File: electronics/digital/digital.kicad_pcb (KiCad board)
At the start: 2 copper layers, 75 parts, among them J1 USB_A, J2 USB_A, J3 RJ45, P1 POWER_IN, P10 AMP_POWER_OUT, P11 CONTROL, P12 ADC, P2 3V3_IN, P3 USB_CABLE, P4 USB_CABLE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

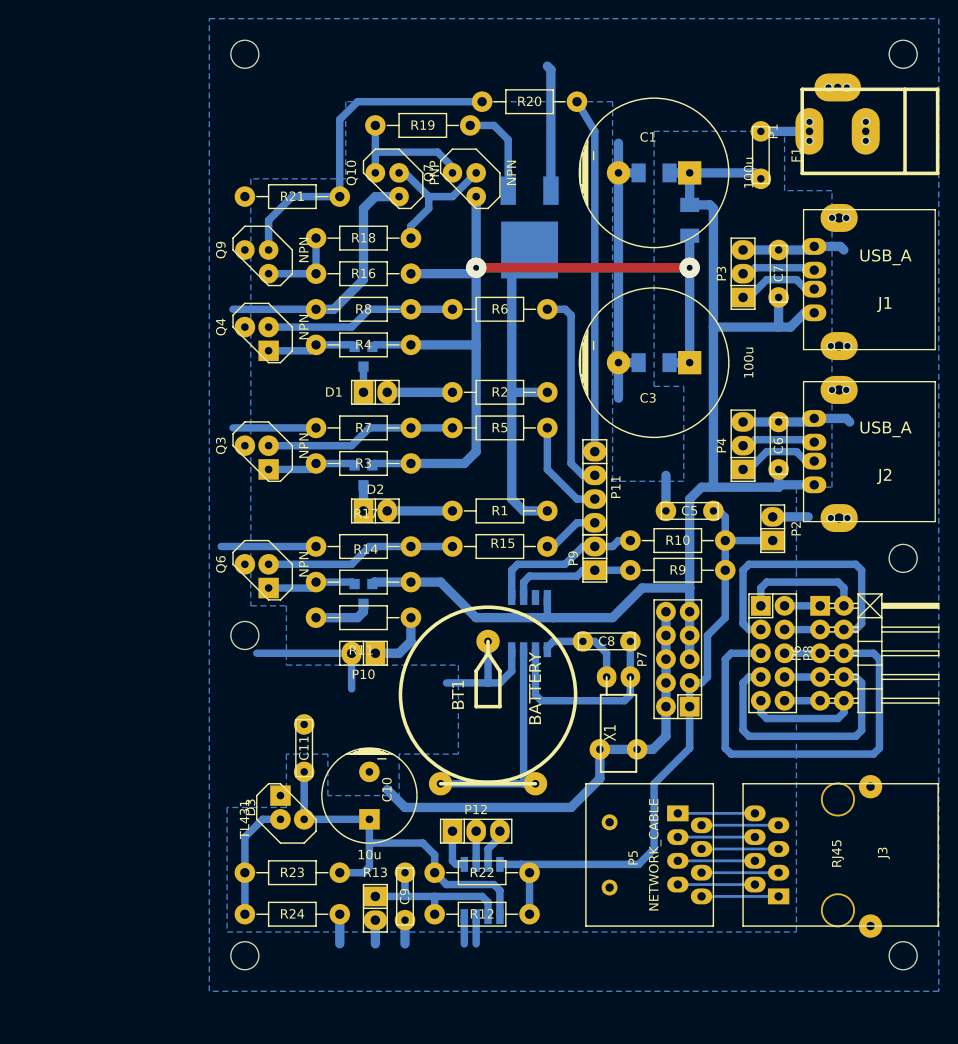
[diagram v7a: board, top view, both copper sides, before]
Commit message: make holes connected to gnd
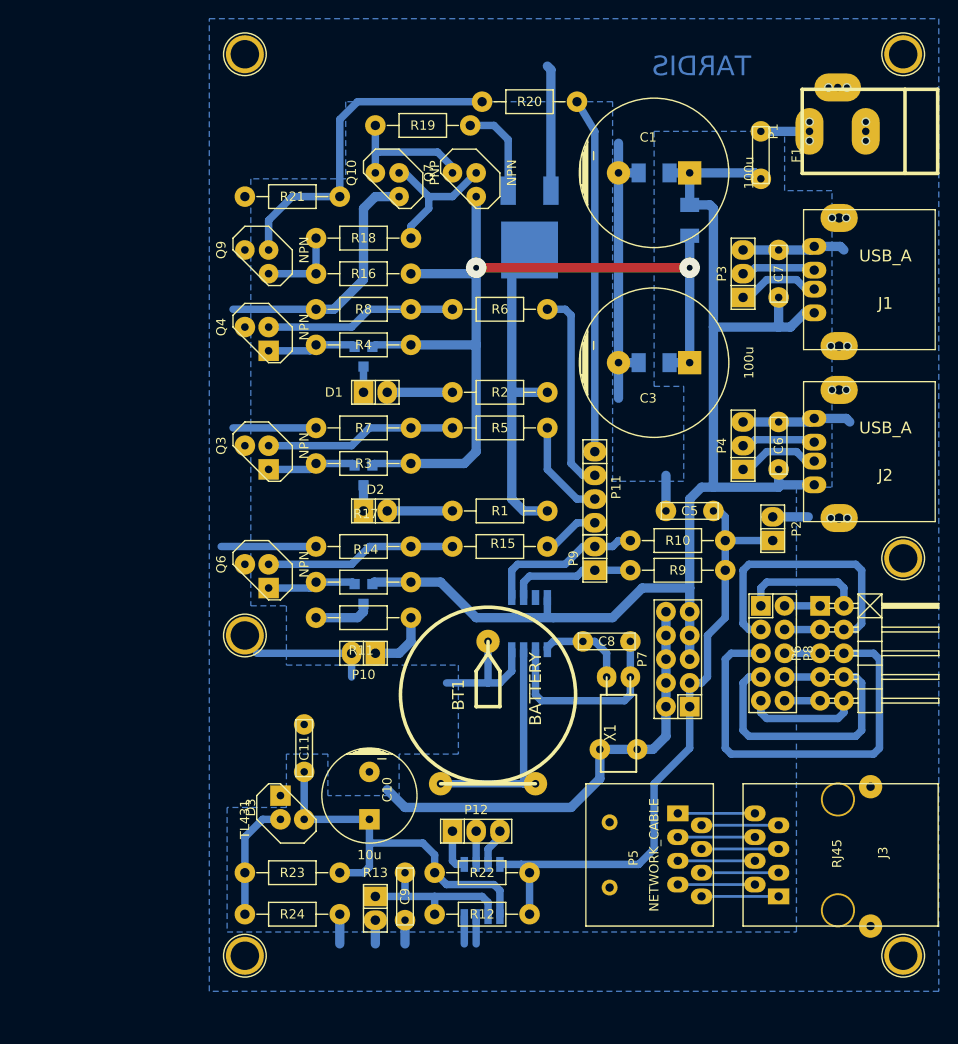
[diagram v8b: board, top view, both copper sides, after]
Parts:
- removed MountingHole_3mm (x6): VAL**, Mounting_Holes:MountingHole_3mm
- added 1pin: VAL**, Connect:1pin, F.Cu at (261.0, 52.7)
- added 1pin: VAL**, Connect:1pin, F.Cu at (261.0, 106.7)
- added 1pin: VAL**, Connect:1pin, F.Cu at (261.0, 149.2)
- added 1pin: VAL**, Connect:1pin, F.Cu at (190.5, 149.2)
- added 1pin: VAL**, Connect:1pin, F.Cu at (190.5, 114.9)
- added 1pin: VAL**, Connect:1pin, F.Cu at (190.5, 52.7)
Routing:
- net GND: track 213.2 -> 211.9 mm
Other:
- board text added: "TARDIS"
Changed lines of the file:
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@@
 (kicad_pcb (version 4) (host pcbnew "(after 2015-jan-16 BZR unknown)-product")
   (general
-    (links 156)
+    (links 162)
     (no_connects 5)
-    (area 186.69 52.705 264.870001 149.365)
+    (area 186.69 48.732 264.870001 153.035001)
     (thickness 1.6)
-    (drawings 0)
+    (drawings 1)
     (tracks 332)
     (zones 0)
@@
     (mod_text_size 1 1)
     (mod_text_width 0.15)
-    (pad_size 3.64998 3.64998)
-    (pad_drill 3.2512)
+    (pad_size 4.064 4.064)
+    (pad_drill 3.048)
     (pad_to_mask_clearance 0)
     (aux_axis_origin 0 0)
@@
     (visible_elements FFFEFF7F)
     (pcbplotparams
-      (layerselection 0x00030_80000001)
+      (layerselection 0x00000_80000000)
       (usegerberextensions false)
       (excludeedgelayer true)
@@
       (padsonsilk false)
       (subtractmaskfromsilk false)
-      (outputformat 1)
+      (outputformat 5)
       (mirror false)
       (drillshape 1)
       (scaleselection 1)
-      (outputdirectory ""))
+      (outputdirectory prints/))
   )
   (net 0 "")
@@
       (net 5 +3.3VP))
   )
-  (module Mounting_Holes:MountingHole_3mm (layer F.Cu)
+  (module Connect:1pin (layer F.Cu)
+    (at 260.985 52.705)
+    (descr "module 1 pin (ou trou mecanique de percage)")
+    (tags DEV)
+    (fp_text reference 1pin (at 0 -3.048) (layer F.SilkS) hide
+      (effects (font (size 1 1) (thickness 0.15)))
+    )
+    (fp_text value VAL** (at 0 2.794) (layer F.SilkS) hide
+      (effects (font (size 1 1) (thickness 0.15)))
+    )
+    (fp_circle (center 0 0) (end 0 -2.286) (layer F.SilkS) (width 0.15))
+    (pad 1 thru_hole circle (at 0 0) (size 4.064 4.064) (drill 3.048) (layers *.Cu *.Mask F.SilkS)
+      (net 2 GND) (zone_connect 2))
+  )
+  (module Connect:1pin (layer F.Cu)
     (at 260.985 106.68)
-    (descr "Mounting hole, Befestigungsbohrung, 3mm, No Annular, Kein Restring,")
-    (tags "Mounting hole, Befestigungsbohrung, 3mm, No Annular, Kein Restring,")
-    (fp_text reference MountingHole_3mm (at 0 -4.0005) (layer F.SilkS) hide
-      (effects (font (size 1 1) (thickness 0.15)))
-    )
-    (fp_text value VAL** (at 1.00076 5.00126) (layer F.SilkS) hide
-      (effects (font (size 1 1) (thickness 0.15)))
-    )
-    (fp_circle (center 0 0) (end 2.99974 0) (layer Cmts.User) (width 0.381))
-    (pad 1 thru_hole circle (at 0 0) (size 2.99974 2.99974) (drill 2.99974) (layers))
-  )
-  (module Mounting_Holes:MountingHole_3mm (layer F.Cu)
+    (descr "module 1 pin (ou trou mecanique de percage)")
+    (tags DEV)
+    (fp_text reference 1pin (at 0 -3.048) (layer F.SilkS) hide
+      (effects (font (size 1 1) (thickness 0.15)))
+    )
+    (fp_text value VAL** (at 0 2.794) (layer F.SilkS) hide
+      (effects (font (size 1 1) (thickness 0.15)))
+    )
+    (fp_circle (center 0 0) (end 0 -2.286) (layer F.SilkS) (width 0.15))
+    (pad 1 thru_hole circle (at 0 0) (size 4.064 4.064) (drill 3.048) (layers *.Cu *.Mask F.SilkS)
+      (net 2 GND) (zone_connect 2))
+  )
+  (module Connect:1pin (layer F.Cu)
     (at 260.985 149.225)
-    (descr "Mounting hole, Befestigungsbohrung, 3mm, No Annular, Kein Restring,")
-    (tags "Mounting hole, Befestigungsbohrung, 3mm, No Annular, Kein Restring,")
-    (fp_text reference MountingHole_3mm (at 0 -4.0005) (layer F.SilkS) hide
-      (effects (font (size 1 1) (thickness 0.15)))
-    )
-    (fp_text value VAL** (at 1.00076 5.00126) (layer F.SilkS) hide
-      (effects (font (size 1 1) (thickness 0.15)))
-    )
-    (fp_circle (center 0 0) (end 2.99974 0) (layer Cmts.User) (width 0.381))
-    (pad 1 thru_hole circle (at 0 0) (size 2.99974 2.99974) (drill 2.99974) (layers))
-  )
-  (module Mounting_Holes:MountingHole_3mm (layer F.Cu)
+    (descr "module 1 pin (ou trou mecanique de percage)")
+    (tags DEV)
+    (fp_text reference 1pin (at 0 -3.048) (layer F.SilkS) hide
+      (effects (font (size 1 1) (thickness 0.15)))
+    )
+    (fp_text value VAL** (at 0 2.794) (layer F.SilkS) hide
+      (effects (font (size 1 1) (thickness 0.15)))
+    )
+    (fp_circle (center 0 0) (end 0 -2.286) (layer F.SilkS) (width 0.15))
+    (pad 1 thru_hole circle (at 0 0) (size 4.064 4.064) (drill 3.048) (layers *.Cu *.Mask F.SilkS)
+      (net 2 GND) (zone_connect 2))
+  )
+  (module Connect:1pin (layer F.Cu)
+    (at 190.5 149.225)
+    (descr "module 1 pin (ou trou mecanique de percage)")
+    (tags DEV)
+    (fp_text reference 1pin (at 0 -3.048) (layer F.SilkS) hide
+      (effects (font (size 1 1) (thickness 0.15)))
+    )
+    (fp_text value VAL** (at 0 2.794) (layer F.SilkS) hide
+      (effects (font (size 1 1) (thickness 0.15)))
+    )
+    (fp_circle (center 0 0) (end 0 -2.286) (layer F.SilkS) (width 0.15))
+    (pad 1 thru_hole circle (at 0 0) (size 4.064 4.064) (drill 3.048) (layers *.Cu *.Mask F.SilkS)
+      (net 2 GND) (zone_connect 2))
+  )
+  (module Connect:1pin (layer F.Cu)
+    (at 190.5 114.935)
+    (descr "module 1 pin (ou trou mecanique de percage)")
+    (tags DEV)
+    (fp_text reference 1pin (at 0 -3.048) (layer F.SilkS) hide
+      (effects (font (size 1 1) (thickness 0.15)))
+    )
+    (fp_text value VAL** (at 0 2.794) (layer F.SilkS) hide
+      (effects (font (size 1 1) (thickness 0.15)))
+    )
+    (fp_circle (center 0 0) (end 0 -2.286) (layer F.SilkS) (width 0.15))
+    (pad 1 thru_hole circle (at 0 0) (size 4.064 4.064) (drill 3.048) (layers *.Cu *.Mask F.SilkS)
+      (net 2 GND) (zone_connect 2))
+  )
+  (module Connect:1pin (layer F.Cu)
     (at 190.5 52.705)
-    (descr "Mounting hole, Befestigungsbohrung, 3mm, No Annular, Kein Restring,")
-    (tags "Mounting hole, Befestigungsbohrung, 3mm, No Annular, Kein Restring,")
-    (fp_text reference MountingHole_3mm (at 0 -4.0005) (layer F.SilkS) hide
-      (effects (font (size 1 1) (thickness 0.15)))
-    )
-    (fp_text value VAL** (at 1.00076 5.00126) (layer F.SilkS) hide
-      (effects (font (size 1 1) (thickness 0.15)))
-    )
-    (fp_circle (center 0 0) (end 2.99974 0) (layer Cmts.User) (width 0.381))
-    (pad 1 thru_hole circle (at 0 0) (size 2.99974 2.99974) (drill 2.99974) (layers))
-  )
-  (module Mounting_Holes:MountingHole_3mm (layer F.Cu)
-    (at 190.5 114.935)
-    (descr "Mounting hole, Befestigungsbohrung, 3mm, No Annular, Kein Restring,")
-    (tags "Mounting hole, Befestigungsbohrung, 3mm, No Annular, Kein Restring,")
-    (fp_text reference MountingHole_3mm (at 0 -4.0005) (layer F.SilkS) hide
-      (effects (font (size 1 1) (thickness 0.15)))
-    )
-    (fp_text value VAL** (at 1.00076 5.00126) (layer F.SilkS) hide
-      (effects (font (size 1 1) (thickness 0.15)))
-    )
-    (fp_circle (center 0 0) (end 2.99974 0) (layer Cmts.User) (width 0.381))
-    (pad 1 thru_hole circle (at 0 0) (size 2.99974 2.99974) (drill 2.99974) (layers))
-  )
-  (module Mounting_Holes:MountingHole_3mm (layer F.Cu)
-    (at 190.5 149.225)
-    (descr "Mounting hole, Befestigungsbohrung, 3mm, No Annular, Kein Restring,")
-    (tags "Mounting hole, Befestigungsbohrung, 3mm, No Annular, Kein Restring,")
-    (fp_text reference MountingHole_3mm (at 0 -4.0005) (layer F.SilkS) hide
-      (effects (font (size 1 1) (thickness 0.15)))
-    )
-    (fp_text value VAL** (at 1.00076 5.00126) (layer F.SilkS) hide
-      (effects (font (size 1 1) (thickness 0.15)))
-    )
-    (fp_circle (center 0 0) (end 2.99974 0) (layer Cmts.User) (width 0.381))
-    (pad 1 thru_hole circle (at 0 0) (size 2.99974 2.99974) (drill 2.99974) (layers))
-  )
-  (module Mounting_Holes:MountingHole_3mm (layer F.Cu)
-    (at 260.985 52.705)
-    (descr "Mounting hole, Befestigungsbohrung, 3mm, No Annular, Kein Restring,")
-    (tags "Mounting hole, Befestigungsbohrung, 3mm, No Annular, Kein Restring,")
-    (fp_text reference MountingHole_3mm (at 0 -4.0005) (layer F.SilkS) hide
-      (effects (font (size 1 1) (thickness 0.15)))
-    )
-    (fp_text value VAL** (at 1.00076 5.00126) (layer F.SilkS) hide
-      (effects (font (size 1 1) (thickness 0.15)))
-    )
-    (fp_circle (center 0 0) (end 2.99974 0) (layer Cmts.User) (width 0.381))
-    (pad 1 thru_hole circle (at 0 0) (size 2.99974 2.99974) (drill 2.99974) (layers))
+    (descr "module 1 pin (ou trou mecanique de percage)")
+    (tags DEV)
+    (fp_text reference 1pin (at 0 -3.048) (layer F.SilkS) hide
+      (effects (font (size 1 1) (thickness 0.15)))
+    )
+    (fp_text value VAL** (at 0 2.794) (layer F.SilkS) hide
+      (effects (font (size 1 1) (thickness 0.15)))
+    )
+    (fp_circle (center 0 0) (end 0 -2.286) (layer F.SilkS) (width 0.15))
+    (pad 1 thru_hole circle (at 0 0) (size 4.064 4.064) (drill 3.048) (layers *.Cu *.Mask F.SilkS)
+      (net 2 GND) (zone_connect 2))
+  )
+  (gr_text "TARDIS\n" (at 239.395 53.975) (layer B.Cu)
+    (effects (font (size 2.1 2.1) (thickness 0.42)) (justify mirror))
   )
   (segment (start 221.615 130.81) (end 220.345 130.81) (width 0.8) (layer B.Cu) (net 1))
@@
   (segment (start 213.995 145.034) (end 213.995 147.955) (width 0.8) (layer B.Cu) (net 2))
   (segment (start 215.265 145.034) (end 215.265 147.955) (width 0.8) (layer B.Cu) (net 2))
-  (segment (start 201.93 116.84) (end 201.93 120.65) (width 0.8) (layer B.Cu) (net 2))
+  (segment (start 201.93 116.84) (end 201.93 119.38) (width 0.8) (layer B.Cu) (net 2))
   (segment (start 198.12 80.01) (end 189.23 80.01) (width 0.8) (layer B.Cu) (net 2))
   (segment (start 198.12 92.71) (end 189.23 92.71) (width 0.8) (layer B.Cu) (net 2))
